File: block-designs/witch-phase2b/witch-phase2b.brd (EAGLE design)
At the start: 134.3 x 85.8 mm, 61 parts, among them IC1 74HC160N, IC10 74LS73N, IC11 74LS08N, IC12 74LS32N, IC2 4511N, IC3 74HC160N, IC4 4511N, IC5 74HC160N, IC6 4511N, IC7 74HC160N, IC8 4511N, IC9 74LS73N

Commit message: updated layouts
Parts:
- added R33, R34, R35, R36: (no value), resistor:0204/5
- added S1, S2, S3, S4: (no value), SparkFun-Electromechanical:TACTILE-PTH
- C12, C3, C6, C9: device resistor:E2-5 -> resistor:C025-025X050
- moved IC12 92.7 mm to (27.9, 16.3)
- moved C12 48.9 mm to (93.2, 23.1), turned to 270 degrees
- moved C9 42.5 mm to (104.4, 23.1), turned to 270 degrees
- moved C3 37.3 mm to (126.7, 22.6)
- moved IC11 37.1 mm to (65.5, 16.0)
- moved C6 36.7 mm to (115.6, 22.9), turned to 270 degrees
- moved IC9 12.2 mm to (48.5, 16.0)
- moved JP1 2.87 mm to (8.13, 42.7)
- moved IC10 0.92 mm to (82.0, 16.0), turned to 90 degrees
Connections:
- removed net N$28: IC3.15, R16.2
- removed net N$29: IC3.1
- removed net N$49: IC5.2
- removed net N$50: IC5.15, R24.2
- removed net N$51: IC5.1
- removed net N$71: IC7.2
- removed net N$72: IC7.15, R32.2
- removed net N$73: IC7.1
- removed net VDD: C1.1, C10.1, C11.1, C12.+, C2.1, C3.+, C4.1, C5.1, C6.+, C7.1, C8.1, C9.+, IC1.10, IC1.16, IC1.7, IC1.9, IC2.16, IC2.3, IC2.4, IC3.10, IC3.16, IC3.7, IC3.9, IC4.16, IC4.3, IC4.4, IC5.10, IC5.16, IC5.7, IC5.9, IC6.16, IC6.3, IC6.4, IC7.10, IC7.16, IC7.7, IC7.9, IC8.16, IC8.3, IC8.4
- removed net VSS: C1.2, C10.2, C11.2, C12.-, C2.2, C3.-, C4.2, C5.2, C6.-, C7.2, C8.2, C9.-, IC1.8, IC2.5, IC2.8, IC3.8, IC4.5, IC4.8, IC5.8, IC6.5, IC6.8, IC7.8, IC8.5, IC8.8, LED1.3, LED1.8, LED2.3, LED2.8, LED3.3, LED3.8, LED4.3, LED4.8
- new net BUTTON0: C3.2, IC12.10, R33.2, S1.3, S1.4
- new net BUTTON1: C6.2, IC12.13, R34.2, S2.3, S2.4
- new net BUTTON2: C9.2, IC12.2, R35.2, S3.3, S3.4
- new net BUTTON3: C12.2, IC12.5, R36.2, S4.3, S4.4
- new net DK0: IC1.2, IC12.8
- new net DK1: IC12.11, IC3.2
- new net DK2: IC12.3, IC5.2
- new net DK3: IC12.6, IC7.2
- new net DKIN0: IC12.9, JP1.17
- new net DKIN1: IC12.12, JP1.13
- new net DKIN2: IC12.1, JP1.9
- new net DKIN3: IC12.4, JP1.5
- new net DKRESET: IC10.2, IC10.6, IC9.2, IC9.6, JP1.3
- new net PULSES: IC11.1, IC11.12, IC11.4, IC11.9, JP1.4
- new net RESET: IC1.1, IC3.1, IC5.1, IC7.1
- new net VCC1: C6.1
- new net VCC2: C9.1
- new net VCC3: C12.1
- new net ZC0: IC1.15, IC10.5, R8.2
- new net ZC1: IC10.1, IC3.15, R16.2
- new net ZC2: IC5.15, IC9.5, R24.2
- new net ZC3: IC7.15, IC9.1, R32.2
- new net ZCOUT0: IC11.11, JP1.18
- new net ZCOUT1: IC11.8, JP1.14
- new net ZCOUT2: IC11.6, JP1.10
- new net ZCOUT3: IC11.3, JP1.6
- net GND: now also C1.2, C10.2, C11.2, C2.2, C4.2, C5.2, C7.2, C8.2, IC1.8, IC10.10, IC10.3, IC2.5, IC2.8, IC3.8, IC4.5, IC4.8, IC5.8, IC6.5, IC6.8, IC7.8, IC8.5, IC8.8, IC9.10, IC9.3, JP1.19, JP1.20, LED1.3, LED1.8, LED2.3, LED2.8, LED3.3, LED3.8, LED4.3, LED4.8, R33.1, R34.1, R35.1, R36.1
- net N$1: now also IC11.2, IC9.12; no longer IC1.15, R8.2
- net N$2: now also IC11.5, IC9.9; no longer IC1.1
- net N$25: now also IC10.12, IC11.10; no longer IC1.2
- net N$27: now also IC10.9, IC11.13; no longer IC3.2
- net VCC: now also C1.1, C10.1, C11.1, C2.1, C3.1, C4.1, C5.1, C7.1, C8.1, IC1.10, IC1.16, IC1.7, IC1.9, IC10.14, IC10.7, IC2.16, IC2.3, IC2.4, IC3.10, IC3.16, IC3.7, IC3.9, IC4.16, IC4.3, IC4.4, IC5.10, IC5.16, IC5.7, IC5.9, IC6.16, IC6.3, IC6.4, IC7.10, IC7.16, IC7.7, IC7.9, IC8.16, IC8.3, IC8.4, IC9.14, IC9.7, JP1.1, JP1.2, S1.1, S1.2, S2.1, S2.2, S3.1, S3.2, S4.1, S4.2
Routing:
- net BUTTON1: track 0.00 -> 164.2 mm, vias 0 -> 2
- net BUTTON0: track 0.00 -> 161.7 mm, vias 0 -> 1
- net DKRESET: track 0.00 -> 137.6 mm, vias 0 -> 1
- net BUTTON2: track 0.00 -> 133.6 mm, vias 0 -> 2
- net ZCOUT0: track 0.00 -> 128.0 mm
- net PULSES: track 0.00 -> 122.9 mm
- net ZCOUT1: track 0.00 -> 105.0 mm
- net DK0: track 0.00 -> 101.6 mm
- net BUTTON3: track 0.00 -> 94.7 mm
- net ZCOUT3: track 0.00 -> 94.0 mm
- net ZCOUT2: track 0.00 -> 93.1 mm
- net RESET: track 0.00 -> 90.7 mm
- net ZC0: track 0.00 -> 69.1 mm
- net DK1: track 0.00 -> 68.3 mm
- net DKIN0: track 0.00 -> 65.8 mm
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
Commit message: updated board layouts
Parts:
- added C13, C14, C15, C16: (no value), resistor:C025-025X050
- added C17: (no value), resistor:E2-5
- added C18: (no value), resistor:C025-040X050
- added R37: (no value), resistor:0204/5
- moved C4 0.51 mm to (25.1, 37.3), turned to 270 degrees
- moved C11 0.51 mm to (79.5, 52.3), turned to 270 degrees
- moved C7 0.51 mm to (25.1, 52.3), turned to 270 degrees
- moved C5 0.36 mm to (106.9, 37.1), turned to 270 degrees
- moved C2 0.25 mm to (52.3, 37.1), turned to 270 degrees
- moved C8 0.25 mm to (79.5, 37.1), turned to 270 degrees
- moved C10 0.25 mm to (52.3, 52.1), turned to 270 degrees
- turned C1 to 270 degrees
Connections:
- new net VDD: R37.1
- new net VSS: C18.2
- net GND: now also C13.2, C14.2, C15.2, C16.2, C17.-
- net RESET: now also C18.1, R37.2
- net VCC: now also C13.1, C14.1, C15.1, C16.1, C17.+
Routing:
- net RESET: track 90.7 -> 125.7 mm
- net DKRESET: track 137.6 -> 156.5 mm, vias 1 -> 0
- net BUTTON0: track 161.7 -> 147.5 mm
- net DKIN1: track 52.5 -> 58.8 mm
- net DKIN0: track 65.8 -> 72.1 mm
- net PULSES: track 122.9 -> 121.3 mm
- added copper zone on layer 1, net GND
- added copper zone on layer 16, net VCC
- removed copper zone on layer 16, net VDD
- removed copper zone on layer 1, net VSS

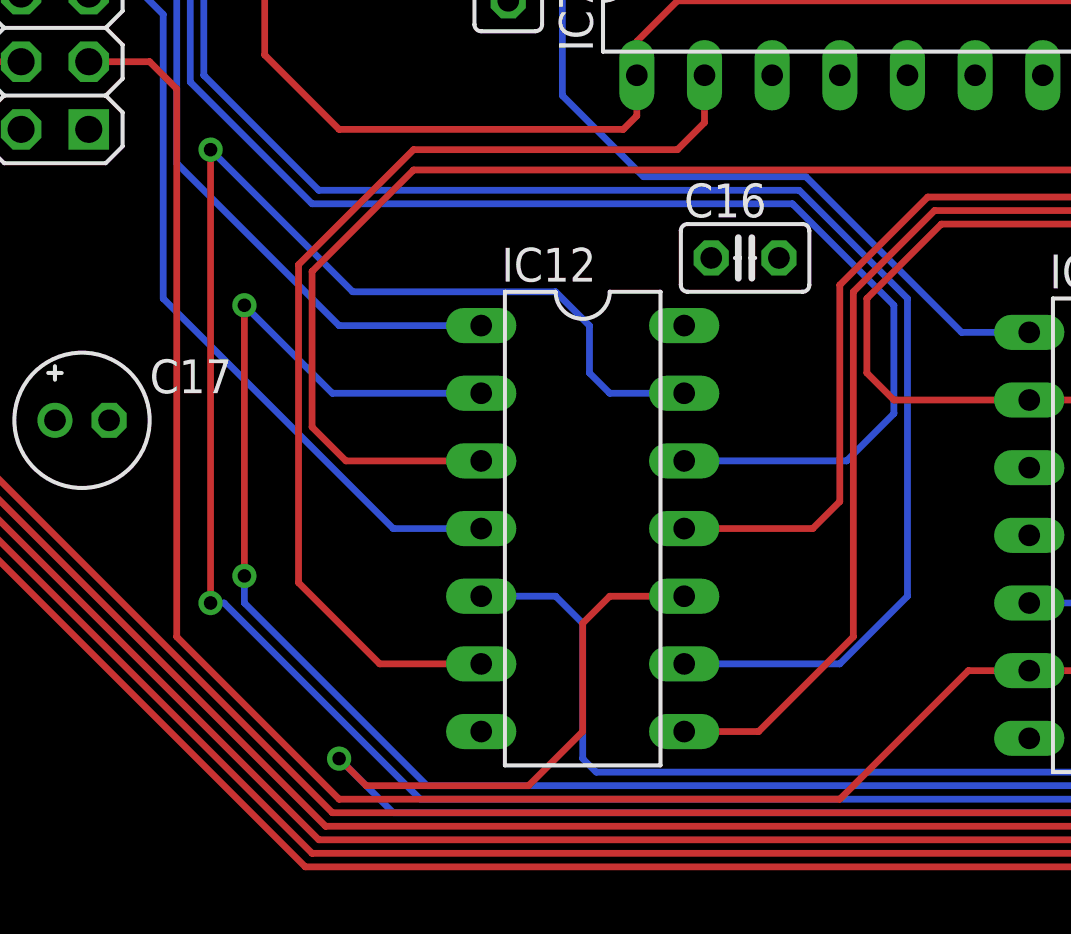
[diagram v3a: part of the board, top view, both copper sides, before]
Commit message: updated figure 4 for the ee article
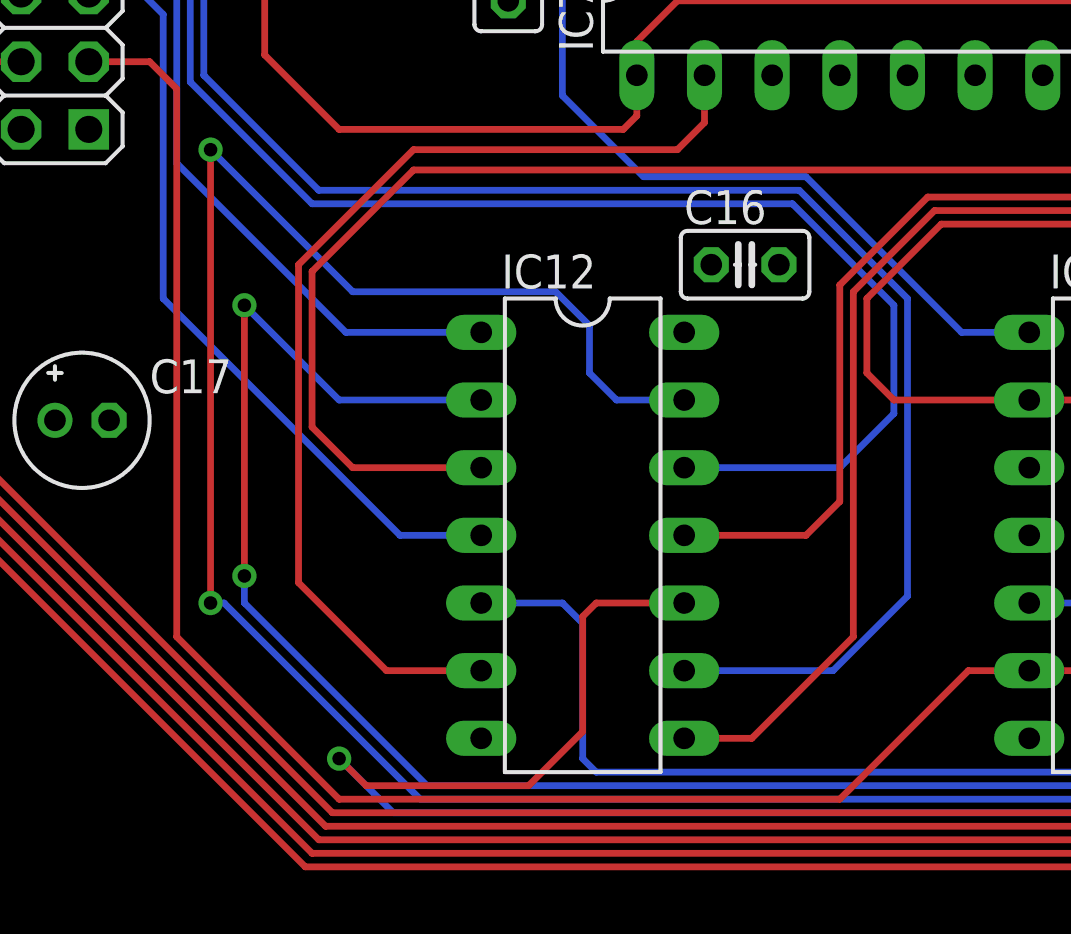
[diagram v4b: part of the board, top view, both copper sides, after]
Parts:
- moved C16 0.25 mm to (34.0, 26.2)
- moved IC12 0.25 mm to (27.9, 16.0)
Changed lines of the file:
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@@
 <element name="IC10" library="74xx-us" package="DIL14" value="74LS73N" x="82.042" y="16.002" rot="R90"/>
 <element name="IC11" library="74xx-us" package="DIL14" value="74LS08N" x="65.532" y="16.002" rot="R270"/>
-<element name="IC12" library="74xx-us" package="DIL14" value="74LS32N" x="27.94" y="16.256" rot="R270"/>
+<element name="IC12" library="74xx-us" package="DIL14" value="74LS32N" x="27.94" y="16.002" rot="R270"/>
 <element name="S1" library="SparkFun-Electromechanical" package="TACTILE-PTH" value="" x="128.27" y="13.208" rot="R90"/>
 <element name="S2" library="SparkFun-Electromechanical" package="TACTILE-PTH" value="" x="117.094" y="13.208" rot="R90"/>
@@
 <element name="C14" library="resistor" package="C025-025X050" value="" x="71.628" y="26.162"/>
 <element name="C15" library="resistor" package="C025-025X050" value="" x="54.61" y="26.162"/>
-<element name="C16" library="resistor" package="C025-025X050" value="" x="34.036" y="26.416"/>
+<element name="C16" library="resistor" package="C025-025X050" value="" x="34.036" y="26.162"/>
 <element name="C17" library="resistor" package="E2-5" value="" x="9.144" y="20.32"/>
 <element name="R37" library="resistor" package="0204/5" value="" x="19.812" y="40.132" rot="R90"/>
@@
 <contactref element="IC1" pad="2"/>
 <contactref element="IC12" pad="8"/>
-<wire x1="31.75" y1="8.636" x2="34.544" y2="8.636" width="0.254" layer="1"/>
-<wire x1="34.544" y1="8.636" x2="38.1" y2="12.192" width="0.254" layer="1"/>
+<wire x1="34.29" y1="8.382" x2="38.1" y2="12.192" width="0.254" layer="1"/>
 <wire x1="38.1" y1="12.192" x2="38.1" y2="25.146" width="0.254" layer="1"/>
 <wire x1="38.1" y1="25.146" x2="41.148" y2="28.194" width="0.254" layer="1"/>
@@
 <wire x1="111.506" y1="28.194" x2="114.046" y2="30.734" width="0.254" layer="1"/>
 <wire x1="114.046" y1="30.734" x2="114.046" y2="33.274" width="0.254" layer="1"/>
+<wire x1="34.29" y1="8.382" x2="31.75" y2="8.382" width="0.254" layer="1"/>
 </signal>
 <signal name="ZC0">
@@
 <contactref element="IC3" pad="2"/>
 <contactref element="IC12" pad="11"/>
-<wire x1="31.75" y1="16.256" x2="36.576" y2="16.256" width="0.254" layer="1"/>
-<wire x1="36.576" y1="16.256" x2="37.592" y2="17.272" width="0.254" layer="1"/>
+<wire x1="36.322" y1="16.002" x2="37.592" y2="17.272" width="0.254" layer="1"/>
 <wire x1="37.592" y1="17.272" x2="37.592" y2="25.4" width="0.254" layer="1"/>
 <wire x1="37.592" y1="25.4" x2="40.894" y2="28.702" width="0.254" layer="1"/>
@@
 <wire x1="84.582" y1="28.702" x2="86.868" y2="30.988" width="0.254" layer="1"/>
 <wire x1="86.868" y1="30.988" x2="86.868" y2="33.274" width="0.254" layer="1"/>
+<wire x1="36.322" y1="16.002" x2="31.75" y2="16.002" width="0.254" layer="1"/>
 </signal>
 <signal name="ZC1">
@@
 <contactref element="IC5" pad="2"/>
 <contactref element="IC12" pad="3"/>
-<wire x1="24.13" y1="18.796" x2="19.05" y2="18.796" width="0.254" layer="1"/>
-<wire x1="19.05" y1="18.796" x2="17.78" y2="20.066" width="0.254" layer="1"/>
+<wire x1="19.304" y1="18.542" x2="17.78" y2="20.066" width="0.254" layer="1"/>
 <wire x1="17.78" y1="20.066" x2="17.78" y2="25.908" width="0.254" layer="1"/>
 <wire x1="17.78" y1="25.908" x2="21.59" y2="29.718" width="0.254" layer="1"/>
@@
 <wire x1="58.166" y1="29.718" x2="59.69" y2="31.242" width="0.254" layer="1"/>
 <wire x1="59.69" y1="31.242" x2="59.69" y2="33.274" width="0.254" layer="1"/>
+<wire x1="19.304" y1="18.542" x2="24.13" y2="18.542" width="0.254" layer="1"/>
 </signal>
 <signal name="ZC2">
@@
 <contactref element="IC7" pad="2"/>
 <contactref element="IC12" pad="6"/>
-<wire x1="24.13" y1="11.176" x2="20.32" y2="11.176" width="0.254" layer="1"/>
-<wire x1="20.32" y1="11.176" x2="17.272" y2="14.224" width="0.254" layer="1"/>
+<wire x1="20.574" y1="10.922" x2="17.272" y2="14.224" width="0.254" layer="1"/>
 <wire x1="17.272" y1="14.224" x2="17.272" y2="26.162" width="0.254" layer="1"/>
 <wire x1="17.272" y1="26.162" x2="21.59" y2="30.48" width="0.254" layer="1"/>
@@
 <wire x1="31.496" y1="30.48" x2="32.512" y2="31.496" width="0.254" layer="1"/>
 <wire x1="32.512" y1="31.496" x2="32.512" y2="33.274" width="0.254" layer="1"/>
+<wire x1="20.574" y1="10.922" x2="24.13" y2="10.922" width="0.254" layer="1"/>
 </signal>
 <signal name="ZC3">
@@
 <wire x1="11.43" y1="36.322" x2="12.192" y2="35.56" width="0.254" layer="16"/>
 <wire x1="12.192" y1="35.56" x2="12.192" y2="24.892" width="0.254" layer="16"/>
-<wire x1="12.192" y1="24.892" x2="20.828" y2="16.256" width="0.254" layer="16"/>
-<wire x1="20.828" y1="16.256" x2="24.13" y2="16.256" width="0.254" layer="16"/>
+<wire x1="12.192" y1="24.892" x2="21.082" y2="16.002" width="0.254" layer="16"/>
+<wire x1="21.082" y1="16.002" x2="24.13" y2="16.002" width="0.254" layer="16"/>
 </signal>
 <signal name="DKIN2">
@@
 <wire x1="11.176" y1="41.402" x2="12.7" y2="39.878" width="0.254" layer="16"/>
 <wire x1="12.7" y1="39.878" x2="12.7" y2="29.972" width="0.254" layer="16"/>
-<wire x1="12.7" y1="29.972" x2="18.796" y2="23.876" width="0.254" layer="16"/>
-<wire x1="18.796" y1="23.876" x2="24.13" y2="23.876" width="0.254" layer="16"/>
+<wire x1="12.7" y1="29.972" x2="19.05" y2="23.622" width="0.254" layer="16"/>
+<wire x1="19.05" y1="23.622" x2="24.13" y2="23.622" width="0.254" layer="16"/>
 </signal>
 <signal name="DKIN1">
@@
 <wire x1="35.814" y1="28.448" x2="39.624" y2="24.638" width="0.254" layer="16"/>
 <wire x1="39.624" y1="24.638" x2="39.624" y2="20.574" width="0.254" layer="16"/>
-<wire x1="39.624" y1="20.574" x2="37.846" y2="18.796" width="0.254" layer="16"/>
-<wire x1="37.846" y1="18.796" x2="31.75" y2="18.796" width="0.254" layer="16"/>
+<wire x1="39.624" y1="20.574" x2="37.592" y2="18.542" width="0.254" layer="16"/>
+<wire x1="37.592" y1="18.542" x2="31.75" y2="18.542" width="0.254" layer="16"/>
 </signal>
 <signal name="DKIN0">
@@
 <wire x1="36.068" y1="28.956" x2="40.132" y2="24.892" width="0.254" layer="16"/>
 <wire x1="40.132" y1="24.892" x2="40.132" y2="13.716" width="0.254" layer="16"/>
-<wire x1="40.132" y1="13.716" x2="37.592" y2="11.176" width="0.254" layer="16"/>
-<wire x1="37.592" y1="11.176" x2="31.75" y2="11.176" width="0.254" layer="16"/>
+<wire x1="40.132" y1="13.716" x2="37.338" y2="10.922" width="0.254" layer="16"/>
+<wire x1="37.338" y1="10.922" x2="31.75" y2="10.922" width="0.254" layer="16"/>
 </signal>
 <signal name="BUTTON3">
@@
 <wire x1="97.0026" y1="16.4592" x2="97.0026" y2="19.7866" width="0.254" layer="16"/>
 <wire x1="97.0026" y1="19.7866" x2="97.028" y2="19.812" width="0.254" layer="16"/>
-<wire x1="24.13" y1="13.716" x2="26.924" y2="13.716" width="0.254" layer="16"/>
-<wire x1="26.924" y1="13.716" x2="27.94" y2="12.7" width="0.254" layer="16"/>
 <wire x1="27.94" y1="12.7" x2="27.94" y2="7.62" width="0.254" layer="16"/>
 <wire x1="27.94" y1="7.62" x2="28.448" y2="7.112" width="0.254" layer="16"/>
@@
 <wire x1="93.218" y1="21.082" x2="94.488" y2="19.812" width="0.254" layer="16"/>
 <wire x1="94.488" y1="19.812" x2="97.028" y2="19.812" width="0.254" layer="16"/>
+<wire x1="27.94" y1="12.7" x2="27.178" y2="13.462" width="0.254" layer="16"/>
+<wire x1="27.178" y1="13.462" x2="24.13" y2="13.462" width="0.254" layer="16"/>
 </signal>
 <signal name="BUTTON2">
 <contactref element="IC12" pad="2"/>
-<wire x1="24.13" y1="21.336" x2="18.542" y2="21.336" width="0.254" layer="16"/>
-<wire x1="18.542" y1="21.336" x2="15.24" y2="24.638" width="0.254" layer="16"/>
+<wire x1="18.796" y1="21.082" x2="15.24" y2="24.638" width="0.254" layer="16"/>
 <via x="15.24" y="24.638" extent="1-16" drill="0.508"/>
 <wire x1="15.24" y1="24.638" x2="15.24" y2="14.478" width="0.254" layer="1"/>
@@
 <wire x1="104.394" y1="20.828" x2="105.664" y2="19.558" width="0.254" layer="16"/>
 <wire x1="105.664" y1="19.558" x2="108.204" y2="19.558" width="0.254" layer="16"/>
+<wire x1="18.796" y1="21.082" x2="24.13" y2="21.082" width="0.254" layer="16"/>
 </signal>
 <signal name="BUTTON1">
@@
 <contactref element="S2" pad="4"/>
 <contactref element="R34" pad="2"/>
-<wire x1="31.75" y1="21.336" x2="28.956" y2="21.336" width="0.254" layer="16"/>
-<wire x1="28.956" y1="21.336" x2="28.194" y2="22.098" width="0.254" layer="16"/>
+<wire x1="29.21" y1="21.082" x2="28.194" y2="22.098" width="0.254" layer="16"/>
 <wire x1="28.194" y1="22.098" x2="28.194" y2="23.876" width="0.254" layer="16"/>
 <wire x1="28.194" y1="23.876" x2="26.924" y2="25.146" width="0.254" layer="16"/>
@@
 <wire x1="115.57" y1="20.828" x2="117.094" y2="19.304" width="0.254" layer="16"/>
 <wire x1="117.094" y1="19.304" x2="119.38" y2="19.304" width="0.254" layer="16"/>
+<wire x1="29.21" y1="21.082" x2="31.75" y2="21.082" width="0.254" layer="16"/>
 </signal>
 <signal name="BUTTON0">
@@
 <wire x1="126.746" y1="20.574" x2="128.016" y2="19.304" width="0.254" layer="16"/>
 <wire x1="128.016" y1="19.304" x2="130.556" y2="19.304" width="0.254" layer="16"/>
-<wire x1="31.75" y1="13.716" x2="28.956" y2="13.716" width="0.254" layer="1"/>
-<wire x1="28.956" y1="13.716" x2="27.94" y2="12.7" width="0.254" layer="1"/>
-<wire x1="27.94" y1="12.7" x2="27.94" y2="8.636" width="0.254" layer="1"/>
+<wire x1="27.94" y1="12.954" x2="27.94" y2="8.636" width="0.254" layer="1"/>
 <wire x1="27.94" y1="8.636" x2="25.908" y2="6.604" width="0.254" layer="1"/>
 <wire x1="25.908" y1="6.604" x2="19.812" y2="6.604" width="0.254" layer="1"/>
@@
 <wire x1="20.828" y1="5.588" x2="126.1618" y2="5.588" width="0.254" layer="16"/>
 <wire x1="126.1618" y1="5.588" x2="130.5306" y2="9.9568" width="0.254" layer="16"/>
+<wire x1="27.94" y1="12.954" x2="28.448" y2="13.462" width="0.254" layer="1"/>
+<wire x1="28.448" y1="13.462" x2="31.75" y2="13.462" width="0.254" layer="1"/>
 </signal>
 <signal name="DKRESET">
